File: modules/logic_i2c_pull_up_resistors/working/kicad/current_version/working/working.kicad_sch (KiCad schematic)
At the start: 2 parts

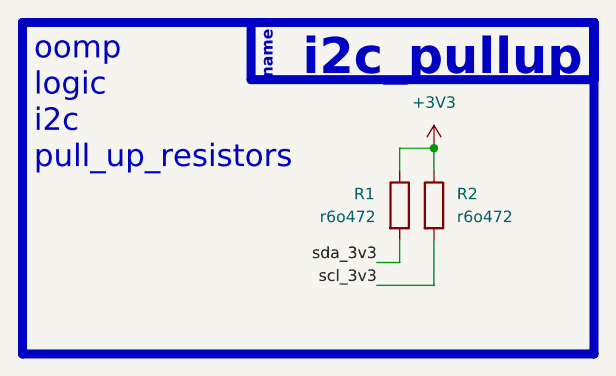
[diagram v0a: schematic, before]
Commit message: fixed formatting to be more consistent
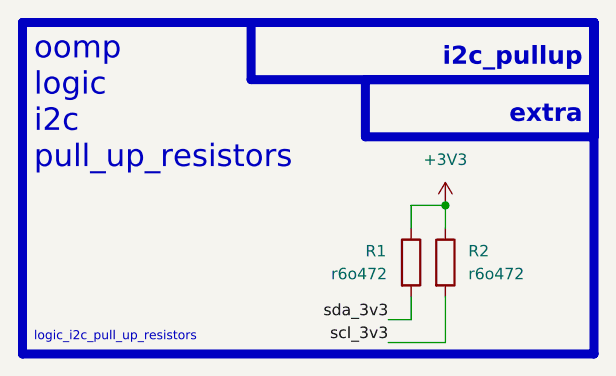
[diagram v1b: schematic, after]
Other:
- note added: "extra"
- note added: "logic_i2c_pull_up_resistors"
- note removed: "name"
- moved on the sheet: R1, R2
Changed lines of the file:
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@@
 (kicad_sch (version 20230121) (generator eeschema)
   (paper "A4")
-  (junction (at 157.48 86.36) (diameter 0) (color 0 0 0 0)
+  (junction (at 158.75 92.71) (diameter 0) (color 0 0 0 0)
   )
-  (wire (pts (xy 157.48 86.36) (xy 157.48 88.9))
+  (wire (pts (xy 158.75 92.71) (xy 158.75 95.25))
     (stroke (width 0) (type default))
   )
-  (wire (pts (xy 157.48 96.52) (xy 157.48 101.6))
+  (wire (pts (xy 158.75 102.87) (xy 158.75 107.95))
     (stroke (width 0) (type default))
   )
-  (wire (pts (xy 157.48 101.6) (xy 151.13 101.6))
+  (wire (pts (xy 158.75 107.95) (xy 152.4 107.95))
     (stroke (width 0) (type default))
   )
-  (wire (pts (xy 151.13 99.06) (xy 153.67 99.06))
+  (wire (pts (xy 152.4 105.41) (xy 154.94 105.41))
     (stroke (width 0) (type default))
   )
-  (wire (pts (xy 153.67 99.06) (xy 153.67 96.52))
+  (wire (pts (xy 154.94 105.41) (xy 154.94 102.87))
     (stroke (width 0) (type default))
   )
-  (wire (pts (xy 157.48 86.36) (xy 153.67 86.36))
+  (wire (pts (xy 158.75 92.71) (xy 154.94 92.71))
     (stroke (width 0) (type default))
   )
-  (wire (pts (xy 153.67 86.36) (xy 153.67 88.9))
+  (wire (pts (xy 154.94 92.71) (xy 154.94 95.25))
     (stroke (width 0) (type default))
   )
@@
   (rectangle (start 137.16 72.39) (end 175.26 78.74)
     (stroke (width 1) (type default))
-    (fill (type color) (color 0 0 0 0))
+    (fill (type none))
   )
-  (text "i2c_pullup\n" (at 173.99 78.74 0)
-    (effects (font (size 4 4) (thickness 0.8) bold (color 255 255 255 1)) (justify right bottom))
+  (rectangle (start 149.86 78.74) (end 175.26 85.09)
+    (stroke (width 1) (type default))
+    (fill (type none))
   )
-  (text "name" (at 139.7 78.74 90)
-    (effects (font (size 1.27 1.27) (thickness 0.254) bold (color 255 255 255 1)) (justify left bottom))
+  (text "i2c_pullup\n" (at 173.99 77.47 0)
+    (effects (font (size 2 2) (thickness 0.8) bold) (justify right bottom))
   )
   (text "oomp\nlogic\ni2c\npull_up_resistors\n" (at 113.03 88.9 0)
     (effects (font (size 2.5 2.5)) (justify left bottom))
   )
-  (label "sda_3v3" (at 151.13 99.06 180) (fields_autoplaced)
+  (text "logic_i2c_pull_up_resistors" (at 113.03 107.95 0)
+    (effects (font (size 1 1)) (justify left bottom))
+  )
+  (text "extra" (at 173.99 83.82 0)
+    (effects (font (size 2 2) (thickness 0.8) bold) (justify right bottom))
+  )
+  (label "sda_3v3" (at 152.4 105.41 180) (fields_autoplaced)
     (effects (font (size 1.27 1.27)) (justify right bottom))
   )
-  (label "scl_3v3" (at 151.13 101.6 180) (fields_autoplaced)
+  (label "scl_3v3" (at 152.4 107.95 180) (fields_autoplaced)
     (effects (font (size 1.27 1.27)) (justify right bottom))
   )
-  (symbol (lib_id "oomlout_oomp_part_symbols:r6o472_electronic_resistor_0603_4700_ohm") (at 157.48 92.71 0) (unit 1)
+  (symbol (lib_id "oomlout_oomp_part_symbols:r6o472_electronic_resistor_0603_4700_ohm") (at 158.75 99.06 0) (unit 1)
     (in_bom yes) (on_board yes) (dnp no)
-    (property "Reference" "R2" (at 160.02 91.44 0)
+    (property "Reference" "R2" (at 161.29 97.79 0)
       (effects (font (size 1.27 1.27)) (justify left))
     )
-    (property "Value" "r6o472" (at 160.02 93.98 0)
+    (property "Value" "r6o472" (at 161.29 100.33 0)
       (effects (font (size 1.27 1.27)) (justify left))
     )
-    (property "Footprint" "oomlout_oomp_part_footprints:r6o472_electronic_resistor_0603_4700_ohm" (at 155.702 92.71 90)
+    (property "Footprint" "oomlout_oomp_part_footprints:r6o472_electronic_resistor_0603_4700_ohm" (at 156.972 99.06 90)
       (effects (font (size 1.27 1.27)) hide)
     )
-    (property "Datasheet" "https://github.com/oomlout/oomlout_oomp_v3/parts/electronic_resistor_0603_4700_ohm/datasheet.pdf" (at 157.48 92.71 0)
+    (property "Datasheet" "https://github.com/oomlout/oomlout_oomp_v3/parts/electronic_resistor_0603_4700_ohm/datasheet.pdf" (at 158.75 99.06 0)
       (effects (font (size 1.27 1.27)) hide)
     )
@@
     )
   )
-  (symbol (lib_id "oomlout_oomp_part_symbols:r6o472_electronic_resistor_0603_4700_ohm") (at 153.67 92.71 0) (unit 1)
+  (symbol (lib_id "oomlout_oomp_part_symbols:r6o472_electronic_resistor_0603_4700_ohm") (at 154.94 99.06 0) (unit 1)
     (in_bom yes) (on_board yes) (dnp no)
-    (property "Reference" "R1" (at 148.59 91.44 0)
+    (property "Reference" "R1" (at 149.86 97.79 0)
       (effects (font (size 1.27 1.27)) (justify left))
     )
-    (property "Value" "r6o472" (at 144.78 93.98 0)
+    (property "Value" "r6o472" (at 146.05 100.33 0)
       (effects (font (size 1.27 1.27)) (justify left))
     )
-    (property "Footprint" "oomlout_oomp_part_footprints:r6o472_electronic_resistor_0603_4700_ohm" (at 151.892 92.71 90)
+    (property "Footprint" "oomlout_oomp_part_footprints:r6o472_electronic_resistor_0603_4700_ohm" (at 153.162 99.06 90)
       (effects (font (size 1.27 1.27)) hide)
     )
-    (property "Datasheet" "https://github.com/oomlout/oomlout_oomp_v3/parts/electronic_resistor_0603_4700_ohm/datasheet.pdf" (at 153.67 92.71 0)
+    (property "Datasheet" "https://github.com/oomlout/oomlout_oomp_v3/parts/electronic_resistor_0603_4700_ohm/datasheet.pdf" (at 154.94 99.06 0)
       (effects (font (size 1.27 1.27)) hide)
     )
@@
     )
   )
-  (symbol (lib_id "power:+3V3") (at 157.48 86.36 0) (unit 1)
+  (symbol (lib_id "power:+3V3") (at 158.75 92.71 0) (unit 1)
     (in_bom yes) (on_board yes) (dnp no) (fields_autoplaced)
-    (property "Reference" "#PWR01" (at 157.48 90.17 0)
+    (property "Reference" "#PWR01" (at 158.75 96.52 0)
       (effects (font (size 1.27 1.27)) hide)
     )
-    (property "Value" "+3V3" (at 157.48 81.28 0)
+    (property "Value" "+3V3" (at 158.75 87.63 0)
       (effects (font (size 1.27 1.27)))
     )
-    (property "Footprint" "" (at 157.48 86.36 0)
+    (property "Footprint" "" (at 158.75 92.71 0)
       (effects (font (size 1.27 1.27)) hide)
     )
-    (property "Datasheet" "" (at 157.48 86.36 0)
+    (property "Datasheet" "" (at 158.75 92.71 0)
       (effects (font (size 1.27 1.27)) hide)
     )

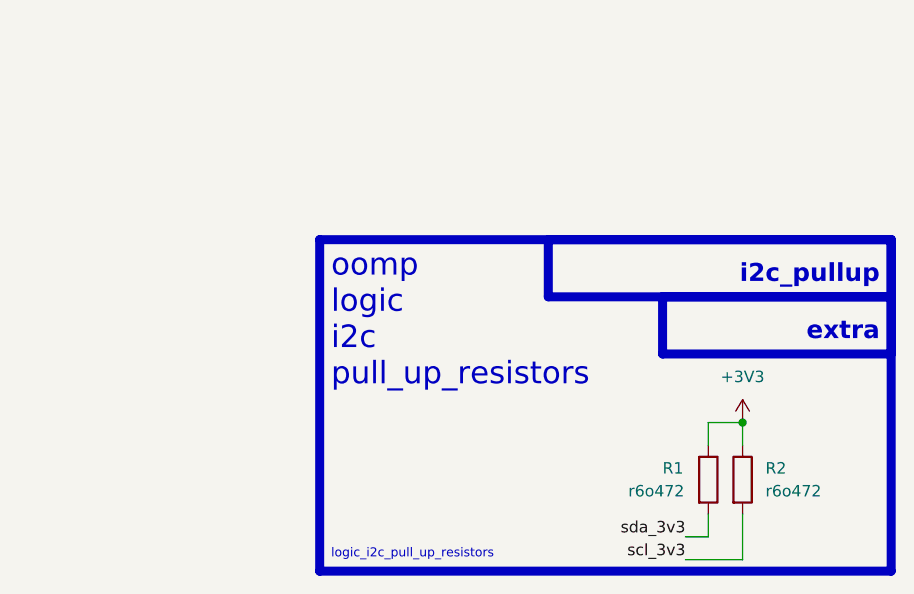
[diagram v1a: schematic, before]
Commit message: schematic formatting
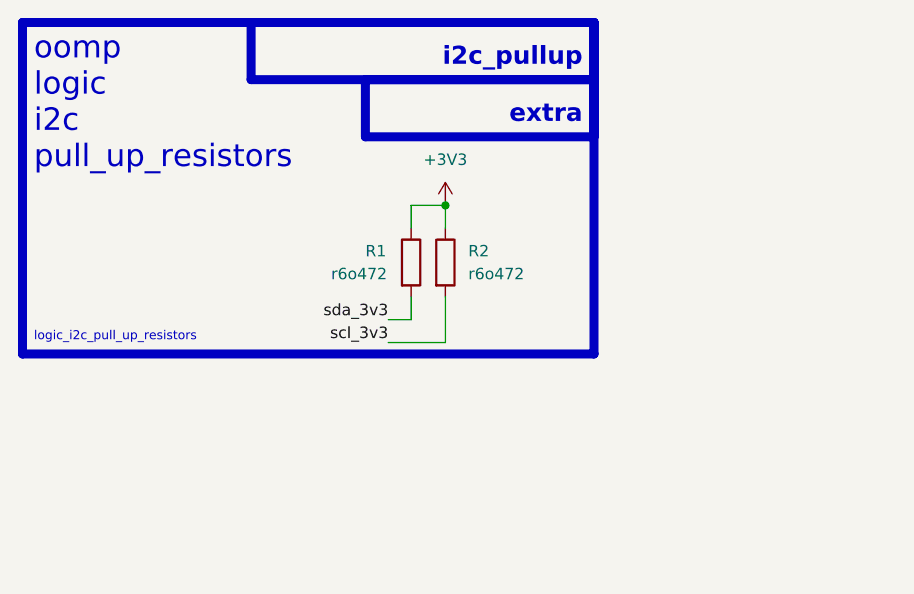
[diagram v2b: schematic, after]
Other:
- moved on the sheet: R1, R2
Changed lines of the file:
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@@
 (kicad_sch (version 20230121) (generator eeschema)
-  (paper "A4")
-  (junction (at 158.75 92.71) (diameter 0) (color 0 0 0 0)
+  (paper "A5")
+  (junction (at 125.73 68.58) (diameter 0) (color 0 0 0 0)
   )
-  (wire (pts (xy 158.75 92.71) (xy 158.75 95.25))
+  (wire (pts (xy 125.73 68.58) (xy 125.73 71.12))
     (stroke (width 0) (type default))
   )
-  (wire (pts (xy 158.75 102.87) (xy 158.75 107.95))
+  (wire (pts (xy 125.73 78.74) (xy 125.73 83.82))
     (stroke (width 0) (type default))
   )
-  (wire (pts (xy 158.75 107.95) (xy 152.4 107.95))
+  (wire (pts (xy 125.73 83.82) (xy 119.38 83.82))
     (stroke (width 0) (type default))
   )
-  (wire (pts (xy 152.4 105.41) (xy 154.94 105.41))
+  (wire (pts (xy 119.38 81.28) (xy 121.92 81.28))
     (stroke (width 0) (type default))
   )
-  (wire (pts (xy 154.94 105.41) (xy 154.94 102.87))
+  (wire (pts (xy 121.92 81.28) (xy 121.92 78.74))
     (stroke (width 0) (type default))
   )
-  (wire (pts (xy 158.75 92.71) (xy 154.94 92.71))
+  (wire (pts (xy 125.73 68.58) (xy 121.92 68.58))
     (stroke (width 0) (type default))
   )
-  (wire (pts (xy 154.94 92.71) (xy 154.94 95.25))
+  (wire (pts (xy 121.92 68.58) (xy 121.92 71.12))
     (stroke (width 0) (type default))
   )
-  (rectangle (start 111.76 72.39) (end 175.26 109.22)
+  (rectangle (start 78.74 48.26) (end 142.24 85.09)
     (stroke (width 1) (type default))
     (fill (type none))
   )
-  (rectangle (start 156.21 236.22) (end 156.21 236.22)
+  (rectangle (start 123.19 212.09) (end 123.19 212.09)
     (stroke (width 0) (type default))
     (fill (type none))
   )
-  (rectangle (start 137.16 72.39) (end 175.26 78.74)
+  (rectangle (start 104.14 48.26) (end 142.24 54.61)
     (stroke (width 1) (type default))
     (fill (type none))
   )
-  (rectangle (start 149.86 78.74) (end 175.26 85.09)
+  (rectangle (start 116.84 54.61) (end 142.24 60.96)
     (stroke (width 1) (type default))
     (fill (type none))
   )
-  (text "i2c_pullup\n" (at 173.99 77.47 0)
+  (text "i2c_pullup\n" (at 140.97 53.34 0)
     (effects (font (size 2 2) (thickness 0.8) bold) (justify right bottom))
   )
-  (text "oomp\nlogic\ni2c\npull_up_resistors\n" (at 113.03 88.9 0)
+  (text "oomp\nlogic\ni2c\npull_up_resistors\n" (at 80.01 64.77 0)
     (effects (font (size 2.5 2.5)) (justify left bottom))
   )
-  (text "logic_i2c_pull_up_resistors" (at 113.03 107.95 0)
+  (text "logic_i2c_pull_up_resistors" (at 80.01 83.82 0)
     (effects (font (size 1 1)) (justify left bottom))
   )
-  (text "extra" (at 173.99 83.82 0)
+  (text "extra" (at 140.97 59.69 0)
     (effects (font (size 2 2) (thickness 0.8) bold) (justify right bottom))
   )
-  (label "sda_3v3" (at 152.4 105.41 180) (fields_autoplaced)
+  (label "sda_3v3" (at 119.38 81.28 180) (fields_autoplaced)
     (effects (font (size 1.27 1.27)) (justify right bottom))
   )
-  (label "scl_3v3" (at 152.4 107.95 180) (fields_autoplaced)
+  (label "scl_3v3" (at 119.38 83.82 180) (fields_autoplaced)
     (effects (font (size 1.27 1.27)) (justify right bottom))
   )
-  (symbol (lib_id "oomlout_oomp_part_symbols:r6o472_electronic_resistor_0603_4700_ohm") (at 158.75 99.06 0) (unit 1)
+  (symbol (lib_id "oomlout_oomp_part_symbols:r6o472_electronic_resistor_0603_4700_ohm") (at 125.73 74.93 0) (unit 1)
     (in_bom yes) (on_board yes) (dnp no)
-    (property "Reference" "R2" (at 161.29 97.79 0)
+    (property "Reference" "R2" (at 128.27 73.66 0)
       (effects (font (size 1.27 1.27)) (justify left))
     )
-    (property "Value" "r6o472" (at 161.29 100.33 0)
+    (property "Value" "r6o472" (at 128.27 76.2 0)
       (effects (font (size 1.27 1.27)) (justify left))
     )
-    (property "Footprint" "oomlout_oomp_part_footprints:r6o472_electronic_resistor_0603_4700_ohm" (at 156.972 99.06 90)
+    (property "Footprint" "oomlout_oomp_part_footprints:r6o472_electronic_resistor_0603_4700_ohm" (at 123.952 74.93 90)
       (effects (font (size 1.27 1.27)) hide)
     )
-    (property "Datasheet" "https://github.com/oomlout/oomlout_oomp_v3/parts/electronic_resistor_0603_4700_ohm/datasheet.pdf" (at 158.75 99.06 0)
+    (property "Datasheet" "https://github.com/oomlout/oomlout_oomp_v3/parts/electronic_resistor_0603_4700_ohm/datasheet.pdf" (at 125.73 74.93 0)
       (effects (font (size 1.27 1.27)) hide)
     )
@@
     )
   )
-  (symbol (lib_id "oomlout_oomp_part_symbols:r6o472_electronic_resistor_0603_4700_ohm") (at 154.94 99.06 0) (unit 1)
+  (symbol (lib_id "oomlout_oomp_part_symbols:r6o472_electronic_resistor_0603_4700_ohm") (at 121.92 74.93 0) (unit 1)
     (in_bom yes) (on_board yes) (dnp no)
-    (property "Reference" "R1" (at 149.86 97.79 0)
+    (property "Reference" "R1" (at 116.84 73.66 0)
       (effects (font (size 1.27 1.27)) (justify left))
     )
-    (property "Value" "r6o472" (at 146.05 100.33 0)
+    (property "Value" "r6o472" (at 113.03 76.2 0)
       (effects (font (size 1.27 1.27)) (justify left))
     )
-    (property "Footprint" "oomlout_oomp_part_footprints:r6o472_electronic_resistor_0603_4700_ohm" (at 153.162 99.06 90)
+    (property "Footprint" "oomlout_oomp_part_footprints:r6o472_electronic_resistor_0603_4700_ohm" (at 120.142 74.93 90)
       (effects (font (size 1.27 1.27)) hide)
     )
-    (property "Datasheet" "https://github.com/oomlout/oomlout_oomp_v3/parts/electronic_resistor_0603_4700_ohm/datasheet.pdf" (at 154.94 99.06 0)
+    (property "Datasheet" "https://github.com/oomlout/oomlout_oomp_v3/parts/electronic_resistor_0603_4700_ohm/datasheet.pdf" (at 121.92 74.93 0)
       (effects (font (size 1.27 1.27)) hide)
     )
@@
     )
   )
-  (symbol (lib_id "power:+3V3") (at 158.75 92.71 0) (unit 1)
+  (symbol (lib_id "power:+3V3") (at 125.73 68.58 0) (unit 1)
     (in_bom yes) (on_board yes) (dnp no) (fields_autoplaced)
-    (property "Reference" "#PWR01" (at 158.75 96.52 0)
+    (property "Reference" "#PWR01" (at 125.73 72.39 0)
       (effects (font (size 1.27 1.27)) hide)
     )
-    (property "Value" "+3V3" (at 158.75 87.63 0)
+    (property "Value" "+3V3" (at 125.73 63.5 0)
       (effects (font (size 1.27 1.27)))
     )
-    (property "Footprint" "" (at 158.75 92.71 0)
+    (property "Footprint" "" (at 125.73 68.58 0)
       (effects (font (size 1.27 1.27)) hide)
     )
-    (property "Datasheet" "" (at 158.75 92.71 0)
+    (property "Datasheet" "" (at 125.73 68.58 0)
       (effects (font (size 1.27 1.27)) hide)
     )
